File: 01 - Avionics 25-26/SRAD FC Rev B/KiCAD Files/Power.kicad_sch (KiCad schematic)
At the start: 0 parts

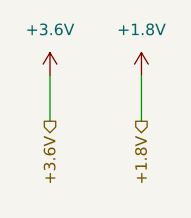
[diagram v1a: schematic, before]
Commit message: wired power on top level sheet
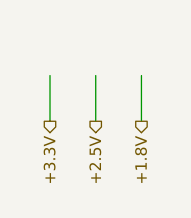
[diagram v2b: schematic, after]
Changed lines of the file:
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@@
+	(wire
+		(pts
+			(xy 97.79 106.68) (xy 97.79 111.76)
+		)
+		(stroke
+			(width 0)
+			(type default)
+		)
+	)
 	(wire
 		(pts
@@
 		)
 	)
+	(hierarchical_label "+3.3V"
+		(shape output)
+		(at 92.71 111.76 270)
+		(effects
+			(font
+				(size 1.27 1.27)
+			)
+			(justify right)
+		)
+	)
 	(hierarchical_label "+1.8V"
 		(shape output)
@@
 		)
 	)
-	(hierarchical_label "+3.6V"
+	(hierarchical_label "+2.5V"
 		(shape output)
-		(at 92.71 111.76 270)
+		(at 97.79 111.76 270)
 		(effects
 			(font
@@
 		)
 	)
-	(symbol
-		(lib_id "power:+3.3V")
-		(at 92.71 106.68 0)
-		(unit 1)
-		(exclude_from_sim no)
-		(in_bom yes)
-		(on_board yes)
-		(dnp no)
-		(fields_autoplaced yes)
-		(property "Reference" "#PWR04"
-			(at 92.71 110.49 0)
-			(effects
-				(font
-					(size 1.27 1.27)
-				)
-				(hide yes)
-			)
-		)
-		(property "Value" "+3.6V"
-			(at 92.71 101.6 0)
-			(effects
-				(font
-					(size 1.27 1.27)
-				)
-			)
-		)
-		(property "Footprint" ""
-			(at 92.71 106.68 0)
-			(effects
-				(font
-					(size 1.27 1.27)
-				)
-				(hide yes)
-			)
-		)
-		(property "Datasheet" ""
-			(at 92.71 106.68 0)
-			(effects
-				(font
-					(size 1.27 1.27)
-				)
-				(hide yes)
-			)
-		)
-		(property "Description" "Power symbol creates a global label with name \"+3.6V\""
-			(at 92.71 106.68 0)
-			(effects
-				(font
-					(size 1.27 1.27)
-				)
-				(hide yes)
-			)
-		)
-		(pin "1"
-		)
-		(instances
-			(project ""
-				(path "/1dd9e63a-24f2-43c6-ae21-66b89e6998f2/6e4b3e58-ab8d-4ff5-b512-9b036522c993"
-					(reference "#PWR04")
-					(unit 1)
-				)
-			)
-		)
-	)
-	(symbol
-		(lib_id "power:+3.3V")
-		(at 102.87 106.68 0)
-		(unit 1)
-		(exclude_from_sim no)
-		(in_bom yes)
-		(on_board yes)
-		(dnp no)
-		(fields_autoplaced yes)
-		(property "Reference" "#PWR05"
-			(at 102.87 110.49 0)
-			(effects
-				(font
-					(size 1.27 1.27)
-				)
-				(hide yes)
-			)
-		)
-		(property "Value" "+1.8V"
-			(at 102.87 101.6 0)
-			(effects
-				(font
-					(size 1.27 1.27)
-				)
-			)
-		)
-		(property "Footprint" ""
-			(at 102.87 106.68 0)
-			(effects
-				(font
-					(size 1.27 1.27)
-				)
-				(hide yes)
-			)
-		)
-		(property "Datasheet" ""
-			(at 102.87 106.68 0)
-			(effects
-				(font
-					(size 1.27 1.27)
-				)
-				(hide yes)
-			)
-		)
-		(property "Description" "Power symbol creates a global label with name \"+1.8V\""
-			(at 102.87 106.68 0)
-			(effects
-				(font
-					(size 1.27 1.27)
-				)
-				(hide yes)
-			)
-		)
-		(pin "1"
-		)
-		(instances
-			(project "SRAD FC Rev B"
-				(path "/1dd9e63a-24f2-43c6-ae21-66b89e6998f2/6e4b3e58-ab8d-4ff5-b512-9b036522c993"
-					(reference "#PWR05")
-					(unit 1)
-				)
-			)
-		)
-	)

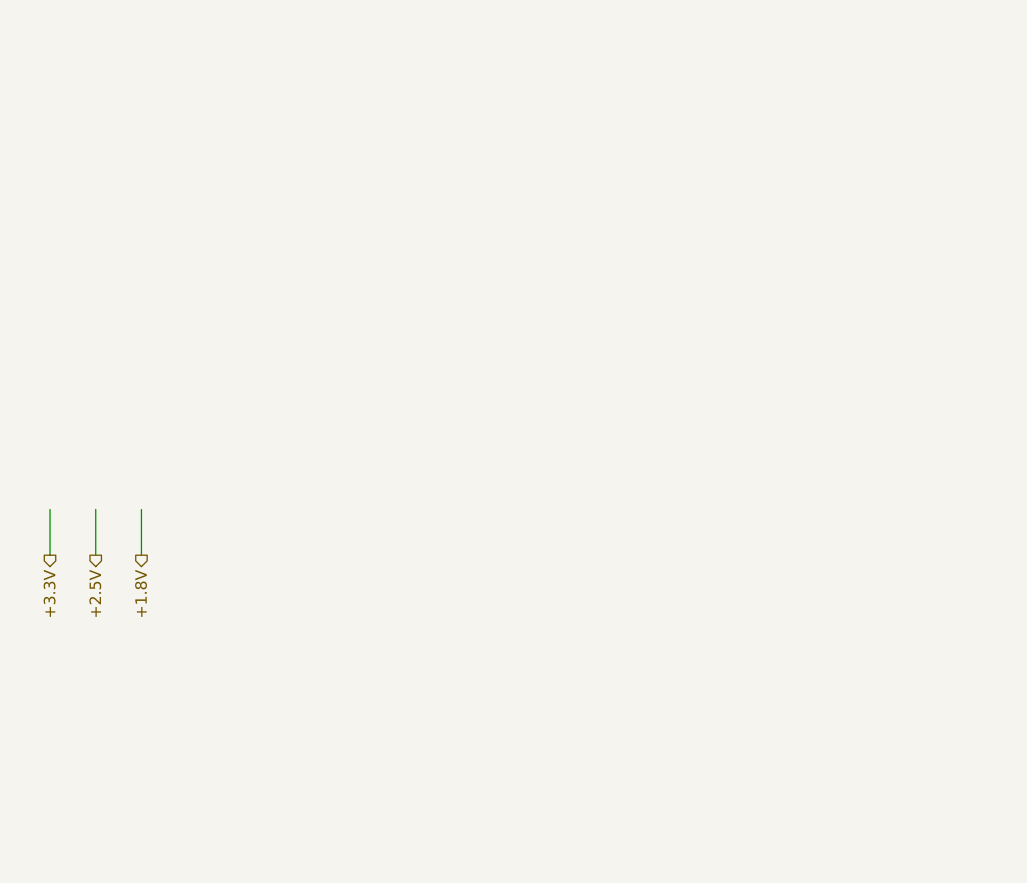
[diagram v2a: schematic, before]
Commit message: set up power conversion, wired power to mcu
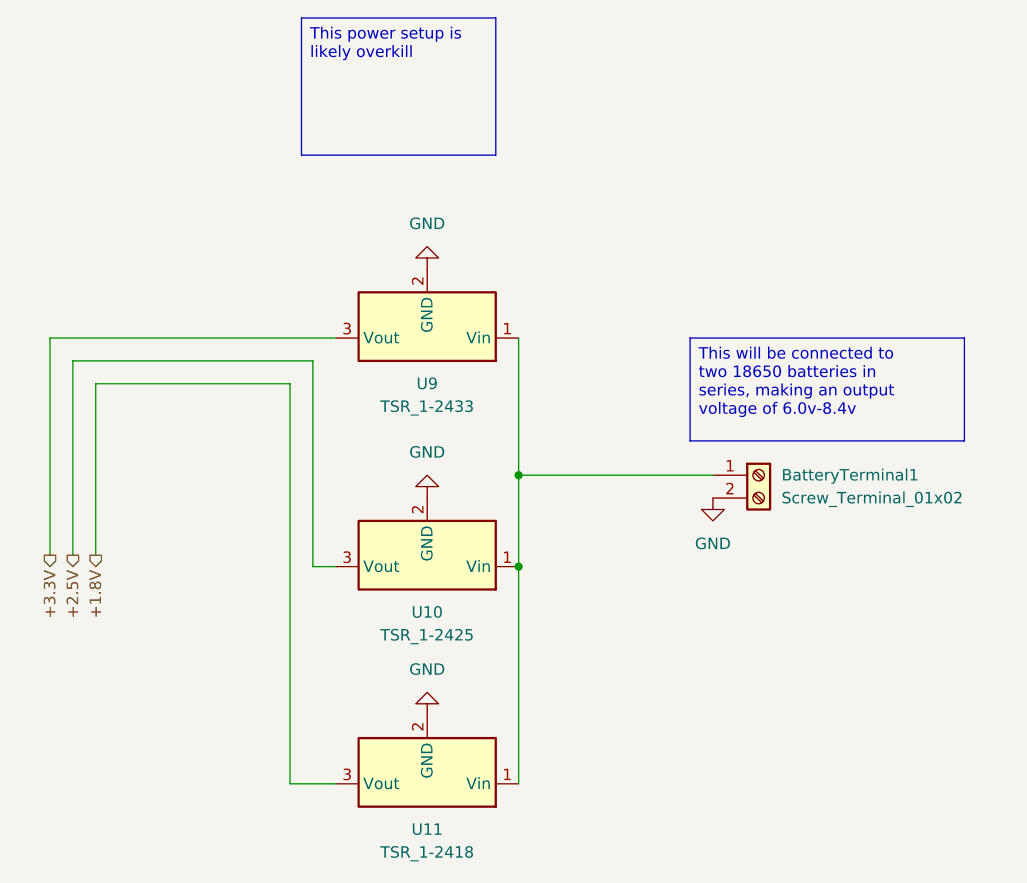
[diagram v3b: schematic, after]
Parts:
- added BatteryTerminal1: Screw_Terminal_01x02, symbol Connector:Screw_Terminal_01x02
- added U10: TSR_1-2425, Converter_DCDC:Converter_DCDC_TRACO_TSR-1_THT, symbol Converter_DCDC:TSR_1-2425
- added U11: TSR_1-2418, Converter_DCDC:Converter_DCDC_TRACO_TSR-1_THT, symbol Converter_DCDC:TSR_1-2418
- added U9: TSR_1-2433, Converter_DCDC:Converter_DCDC_TRACO_TSR-1_THT, symbol Converter_DCDC:TSR_1-2433
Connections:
- net +1.8V: now also U11.3 (Vout)
- net +2.5V: now also U10.3 (Vout)
- net +3.3V: now also U9.3 (Vout)
- new net: BatteryTerminal1.1 (Pin_1), U10.1 (Vin), U11.1 (Vin), U9.1 (Vin)
- new net GND: BatteryTerminal1.2 (Pin_2), U10.2 (GND), U11.2 (GND), U9.2 (GND)

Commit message: some fixes from seth's feedback
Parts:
- removed U10: TSR_1-2425, Converter_DCDC:Converter_DCDC_TRACO_TSR-1_THT, symbol Converter_DCDC:TSR_1-2425
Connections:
- net BAT_RAW: now reaches BatteryTerminal1.1 (Pin_1), U11.1 (Vin), U9.1 (Vin)
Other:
- moved on the sheet: U11
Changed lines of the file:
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@@
 	)
 	(junction
-		(at 144.78 113.03)
+		(at 154.94 102.87)
 		(diameter 0)
 		(color 0 0 0 0)
@@
 	(wire
 		(pts
-			(xy 95.25 90.17) (xy 121.92 90.17)
-		)
-		(stroke
-			(width 0)
-			(type default)
-		)
-	)
-	(wire
-		(pts
-			(xy 121.92 113.03) (xy 124.46 113.03)
-		)
-		(stroke
-			(width 0)
-			(type default)
-		)
-	)
-	(wire
-		(pts
-			(xy 95.25 90.17) (xy 95.25 111.76)
-		)
-		(stroke
-			(width 0)
-			(type default)
-		)
-	)
-	(wire
-		(pts
-			(xy 124.46 137.16) (xy 119.38 137.16)
+			(xy 154.94 102.87) (xy 154.94 109.22)
+		)
+		(stroke
+			(width 0)
+			(type default)
+		)
+	)
+	(wire
+		(pts
+			(xy 124.46 118.11) (xy 119.38 118.11)
 		)
 		(stroke
@@
 	(wire
 		(pts
-			(xy 144.78 113.03) (xy 144.78 137.16)
-		)
-		(stroke
-			(width 0)
-			(type default)
-		)
-	)
-	(wire
-		(pts
 			(xy 124.46 87.63) (xy 92.71 87.63)
 		)
@@
 	(wire
 		(pts
-			(xy 144.78 102.87) (xy 166.37 102.87)
-		)
-		(stroke
-			(width 0)
-			(type default)
-		)
-	)
-	(wire
-		(pts
-			(xy 121.92 90.17) (xy 121.92 113.03)
+			(xy 144.78 102.87) (xy 154.94 102.87)
 		)
 		(stroke
@@
 	(wire
 		(pts
+			(xy 154.94 102.87) (xy 166.37 102.87)
+		)
+		(stroke
+			(width 0)
+			(type default)
+		)
+	)
+	(wire
+		(pts
 			(xy 92.71 87.63) (xy 92.71 111.76)
 		)
@@
 	(wire
 		(pts
-			(xy 144.78 102.87) (xy 144.78 113.03)
-		)
-		(stroke
-			(width 0)
-			(type default)
-		)
-	)
-	(wire
-		(pts
-			(xy 119.38 137.16) (xy 119.38 92.71)
+			(xy 144.78 102.87) (xy 144.78 118.11)
+		)
+		(stroke
+			(width 0)
+			(type default)
+		)
+	)
+	(wire
+		(pts
+			(xy 119.38 118.11) (xy 119.38 92.71)
 		)
 		(stroke
@@
 		)
 	)
-	(hierarchical_label "+2.5V"
+	(hierarchical_label "BAT_RAW"
 		(shape output)
-		(at 95.25 111.76 270)
+		(at 154.94 109.22 270)
 		(effects
 			(font
@@
 	)
 	(symbol
-		(lib_id "power:GND")
-		(at 134.62 105.41 180)
-		(unit 1)
-		(exclude_from_sim no)
-		(in_bom yes)
-		(on_board yes)
-		(dnp no)
-		(fields_autoplaced yes)
-		(property "Reference" "#PWR05"
-			(at 134.62 99.06 0)
-			(effects
-				(font
-					(size 1.27 1.27)
-				)
-				(hide yes)
-			)
-		)
-		(property "Value" "GND"
-			(at 134.62 100.33 0)
-			(effects
-				(font
-					(size 1.27 1.27)
-				)
-			)
-		)
-		(property "Footprint" ""
-			(at 134.62 105.41 0)
-			(effects
-				(font
-					(size 1.27 1.27)
-				)
-				(hide yes)
-			)
-		)
-		(property "Datasheet" ""
-			(at 134.62 105.41 0)
-			(effects
-				(font
-					(size 1.27 1.27)
-				)
-				(hide yes)
-			)
-		)
-		(property "Description" "Power symbol creates a global label with name \"GND\" , ground"
-			(at 134.62 105.41 0)
-			(effects
-				(font
-					(size 1.27 1.27)
-				)
-				(hide yes)
-			)
-		)
-		(pin "1"
-		)
-		(instances
-			(project "SRAD FC Rev B"
-				(path "/1dd9e63a-24f2-43c6-ae21-66b89e6998f2/6e4b3e58-ab8d-4ff5-b512-9b036522c993"
-					(reference "#PWR05")
-					(unit 1)
-				)
-			)
-		)
-	)
-	(symbol
 		(lib_id "Converter_DCDC:TSR_1-2418")
-		(at 134.62 134.62 180)
+		(at 134.62 115.57 180)
 		(unit 1)
 		(exclude_from_sim no)
@@
 		(fields_autoplaced yes)
 		(property "Reference" "U11"
-			(at 134.62 142.24 0)
+			(at 134.62 123.19 0)
 			(effects
 				(font
@@
 		)
 		(property "Value" "TSR_1-2418"
-			(at 134.62 144.78 0)
+			(at 134.62 125.73 0)
 			(effects
 				(font
@@
 		)
 		(property "Footprint" "Converter_DCDC:Converter_DCDC_TRACO_TSR-1_THT"
-			(at 134.62 130.81 0)
+			(at 134.62 111.76 0)
 			(effects
 				(font
@@
 		)
 		(property "Datasheet" "http://www.tracopower.com/products/tsr1.pdf"
-			(at 134.62 134.62 0)
+			(at 134.62 115.57 0)
 			(effects
 				(font
@@
 		)
 		(property "Description" "1A step-down regulator module, fixed 1.8V output voltage, 6-36V input voltage, -40°C to +85°C temperature range, TO-220 compatible LM78xx replacement"
-			(at 134.62 134.62 0)
+			(at 134.62 115.57 0)
 			(effects
 				(font
@@
 	(symbol
 		(lib_id "power:GND")
-		(at 134.62 129.54 180)
+		(at 134.62 110.49 180)
 		(unit 1)
 		(exclude_from_sim no)
@@
 		(fields_autoplaced yes)
 		(property "Reference" "#PWR011"
-			(at 134.62 123.19 0)
+			(at 134.62 104.14 0)
 			(effects
 				(font
@@
 		)
 		(property "Value" "GND"
-			(at 134.62 124.46 0)
+			(at 134.62 105.41 0)
 			(effects
 				(font
@@
 		)
 		(property "Footprint" ""
-			(at 134.62 129.54 0)
+			(at 134.62 110.49 0)
 			(effects
 				(font
@@
 		)
 		(property "Datasheet" ""
-			(at 134.62 129.54 0)
+			(at 134.62 110.49 0)
 			(effects
 				(font
@@
 		)
 		(property "Description" "Power symbol creates a global label with name \"GND\" , ground"
-			(at 134.62 129.54 0)
+			(at 134.62 110.49 0)
 			(effects
 				(font
@@
 					(unit 1)
 				)
-			)
-		)
-	)
-	(symbol
-		(lib_id "Converter_DCDC:TSR_1-2425")
-		(at 134.62 110.49 180)
-		(unit 1)
-		(exclude_from_sim no)
-		(in_bom yes)
-		(on_board yes)
-		(dnp no)
-		(fields_autoplaced yes)
-		(property "Reference" "U10"
-			(at 134.62 118.11 0)
-			(effects
-				(font
-					(size 1.27 1.27)
-				)
-			)
-		)
-		(property "Value" "TSR_1-2425"
-			(at 134.62 120.65 0)
-			(effects
-				(font
-					(size 1.27 1.27)
-				)
-			)
-		)
-		(property "Footprint" "Converter_DCDC:Converter_DCDC_TRACO_TSR-1_THT"
-			(at 134.62 106.68 0)
-			(effects
-				(font
-					(size 1.27 1.27)
-					(italic yes)
-				)
-				(justify left)
-				(hide yes)
-			)
-		)
-		(property "Datasheet" "http://www.tracopower.com/products/tsr1.pdf"
-			(at 134.62 110.49 0)
-			(effects
-				(font
-					(size 1.27 1.27)
-				)
-				(hide yes)
-			)
-		)
-		(property "Description" "1A step-down regulator module, fixed 2.5V output voltage, 6-36V input voltage, -40°C to +85°C temperature range, TO-220 compatible LM78xx replacement"
-			(at 134.62 110.49 0)
-			(effects
-				(font
-					(size 1.27 1.27)
-				)
-				(hide yes)
-			)
-		)
-		(pin "3"
-		)
-		(pin "2"
-		)
-		(pin "1"
-		)
-		(instances
-			(project ""
-				(path "/1dd9e63a-24f2-43c6-ae21-66b89e6998f2/6e4b3e58-ab8d-4ff5-b512-9b036522c993"
-					(reference "U10")
-					(unit 1)
-				)
